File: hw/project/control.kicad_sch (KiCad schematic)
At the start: 46 parts, among them SW1 BOOT0, SW2 RESET, U1 STSPIN32G4, X1 32MHZ 10PF

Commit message: Place next tier of components after critical ones
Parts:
- removed TP4: REGIN, TestPoint:TestPoint_Pad_D1.0mm, symbol Connector:TestPoint
- removed TP8: VBAT, TestPoint:TestPoint_Pad_D1.0mm, symbol Connector:TestPoint
- renumbered TP2 to TP1, TP3 to TP2, TP5 to TP3, TP6 to TP4, TP7 to TP5, TP9 to TP6, TP10 to TP7, TP11 to TP8
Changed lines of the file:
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@@
 		(dnp no)
 		(fields_autoplaced yes)
-		(property "Reference" "TP6"
+		(property "Reference" "TP4"
 			(at 195.58 74.93 0)
 			(show_name no)
@@
 			(project "esc"
 				(path "/86a17c4d-db96-42a1-af84-d43fe593f4e6/50f7e8ea-49d2-4d3d-890c-dc3d94742dd9"
-					(reference "TP6")
+					(reference "TP4")
 					(unit 1)
 				)
@@
 		(dnp no)
 		(fields_autoplaced yes)
-		(property "Reference" "TP2"
+		(property "Reference" "TP1"
 			(at 185.42 29.2099 90)
 			(show_name no)
@@
 			(project "esc"
 				(path "/86a17c4d-db96-42a1-af84-d43fe593f4e6/50f7e8ea-49d2-4d3d-890c-dc3d94742dd9"
-					(reference "TP2")
+					(reference "TP1")
 					(unit 1)
 				)
@@
 		(dnp no)
 		(fields_autoplaced yes)
-		(property "Reference" "TP11"
+		(property "Reference" "TP8"
 			(at 162.56 152.9079 0)
 			(show_name no)
@@
 			(project "esc"
 				(path "/86a17c4d-db96-42a1-af84-d43fe593f4e6/50f7e8ea-49d2-4d3d-890c-dc3d94742dd9"
-					(reference "TP11")
+					(reference "TP8")
 					(unit 1)
 				)
@@
 	(symbol
 		(lib_id "Connector:TestPoint")
-		(at 170.18 68.58 0)
-		(unit 1)
-		(body_style 1)
-		(exclude_from_sim no)
-		(in_bom no)
-		(on_board yes)
-		(in_pos_files yes)
-		(dnp no)
-		(fields_autoplaced yes)
-		(property "Reference" "TP4"
-			(at 172.72 64.0079 0)
-			(show_name no)
-			(do_not_autoplace no)
-			(effects
-				(font
-					(size 1.27 1.27)
-				)
-				(justify left)
-			)
-		)
-		(property "Value" "REGIN"
-			(at 172.72 66.5479 0)
-			(show_name no)
-			(do_not_autoplace no)
-			(effects
-				(font
-					(size 1.27 1.27)
-				)
-				(justify left)
-			)
-		)
-		(property "Footprint" "TestPoint:TestPoint_Pad_D1.0mm"
-			(at 175.26 68.58 0)
-			(hide yes)
-			(show_name no)
-			(do_not_autoplace no)
-			(effects
-				(font
-					(size 1.27 1.27)
-				)
-			)
-		)
-		(property "Datasheet" ""
-			(at 175.26 68.58 0)
-			(hide yes)
-			(show_name no)
-			(do_not_autoplace no)
-			(effects
-				(font
-					(size 1.27 1.27)
-				)
-			)
-		)
-		(property "Description" "test point"
-			(at 170.18 68.58 0)
-			(hide yes)
-			(show_name no)
-			(do_not_autoplace no)
-			(effects
-				(font
-					(size 1.27 1.27)
-				)
-			)
-		)
-		(pin "1"
-		)
-		(instances
-			(project "esc"
-				(path "/86a17c4d-db96-42a1-af84-d43fe593f4e6/50f7e8ea-49d2-4d3d-890c-dc3d94742dd9"
-					(reference "TP4")
-					(unit 1)
-				)
-			)
-		)
-	)
-	(symbol
-		(lib_id "Connector:TestPoint")
 		(at 219.71 68.58 270)
 		(unit 1)
@@
 		(dnp no)
 		(fields_autoplaced yes)
-		(property "Reference" "TP5"
+		(property "Reference" "TP3"
 			(at 224.79 67.3099 90)
 			(show_name no)
@@
 			(project "esc"
 				(path "/86a17c4d-db96-42a1-af84-d43fe593f4e6/50f7e8ea-49d2-4d3d-890c-dc3d94742dd9"
-					(reference "TP5")
+					(reference "TP3")
 					(unit 1)
 				)
@@
 		(dnp no)
 		(fields_autoplaced yes)
-		(property "Reference" "TP10"
+		(property "Reference" "TP7"
 			(at 129.54 152.9079 0)
 			(show_name no)
@@
 			(project "esc"
 				(path "/86a17c4d-db96-42a1-af84-d43fe593f4e6/50f7e8ea-49d2-4d3d-890c-dc3d94742dd9"
-					(reference "TP10")
-					(unit 1)
-				)
-			)
-		)
-	)
-	(symbol
-		(lib_id "Connector:TestPoint")
-		(at 187.96 109.22 0)
-		(unit 1)
-		(body_style 1)
-		(exclude_from_sim no)
-		(in_bom no)
-		(on_board yes)
-		(in_pos_files yes)
-		(dnp no)
-		(fields_autoplaced yes)
-		(property "Reference" "TP8"
-			(at 190.5 104.6479 0)
-			(show_name no)
-			(do_not_autoplace no)
-			(effects
-				(font
-					(size 1.27 1.27)
-				)
-				(justify left)
-			)
-		)
-		(property "Value" "VBAT"
-			(at 190.5 107.1879 0)
-			(show_name no)
-			(do_not_autoplace no)
-			(effects
-				(font
-					(size 1.27 1.27)
-				)
-				(justify left)
-			)
-		)
-		(property "Footprint" "TestPoint:TestPoint_Pad_D1.0mm"
-			(at 193.04 109.22 0)
-			(hide yes)
-			(show_name no)
-			(do_not_autoplace no)
-			(effects
-				(font
-					(size 1.27 1.27)
-				)
-			)
-		)
-		(property "Datasheet" ""
-			(at 193.04 109.22 0)
-			(hide yes)
-			(show_name no)
-			(do_not_autoplace no)
-			(effects
-				(font
-					(size 1.27 1.27)
-				)
-			)
-		)
-		(property "Description" "test point"
-			(at 187.96 109.22 0)
-			(hide yes)
-			(show_name no)
-			(do_not_autoplace no)
-			(effects
-				(font
-					(size 1.27 1.27)
-				)
-			)
-		)
-		(pin "1"
-		)
-		(instances
-			(project "esc"
-				(path "/86a17c4d-db96-42a1-af84-d43fe593f4e6/50f7e8ea-49d2-4d3d-890c-dc3d94742dd9"
-					(reference "TP8")
+					(reference "TP7")
 					(unit 1)
 				)
@@
 		(dnp no)
 		(fields_autoplaced yes)
-		(property "Reference" "TP3"
+		(property "Reference" "TP2"
 			(at 143.51 67.3099 90)
 			(show_name no)
@@
 			(project "esc"
 				(path "/86a17c4d-db96-42a1-af84-d43fe593f4e6/50f7e8ea-49d2-4d3d-890c-dc3d94742dd9"
-					(reference "TP3")
+					(reference "TP2")
 					(unit 1)
 				)
@@
 		(dnp no)
 		(fields_autoplaced yes)
-		(property "Reference" "TP9"
+		(property "Reference" "TP6"
 			(at 147.32 114.3 0)
 			(show_name no)
@@
 			(project "esc"
 				(path "/86a17c4d-db96-42a1-af84-d43fe593f4e6/50f7e8ea-49d2-4d3d-890c-dc3d94742dd9"
-					(reference "TP9")
+					(reference "TP6")
 					(unit 1)
 				)
@@
 		(dnp no)
 		(fields_autoplaced yes)
-		(property "Reference" "TP7"
+		(property "Reference" "TP5"
 			(at 157.48 104.6479 0)
 			(show_name no)
@@
 			(project "esc"
 				(path "/86a17c4d-db96-42a1-af84-d43fe593f4e6/50f7e8ea-49d2-4d3d-890c-dc3d94742dd9"
-					(reference "TP7")
+					(reference "TP5")
 					(unit 1)
 				)

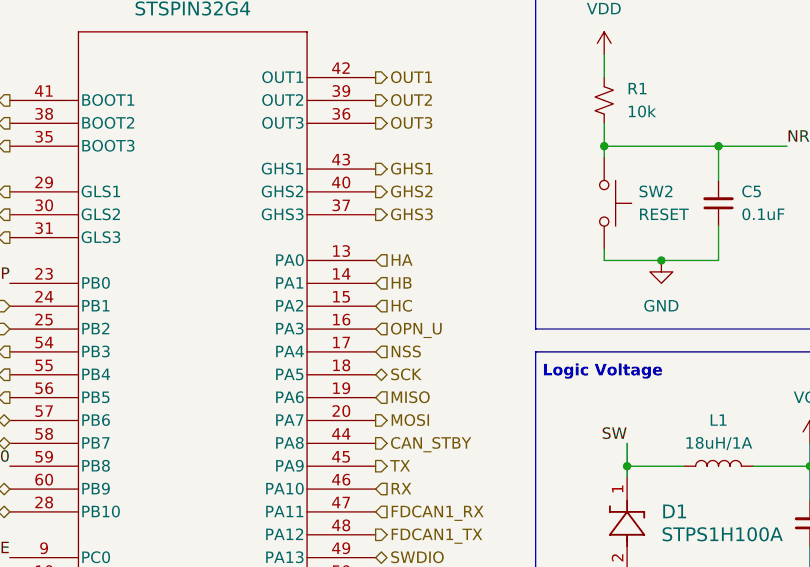
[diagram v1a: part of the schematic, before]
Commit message: Label JST connectors
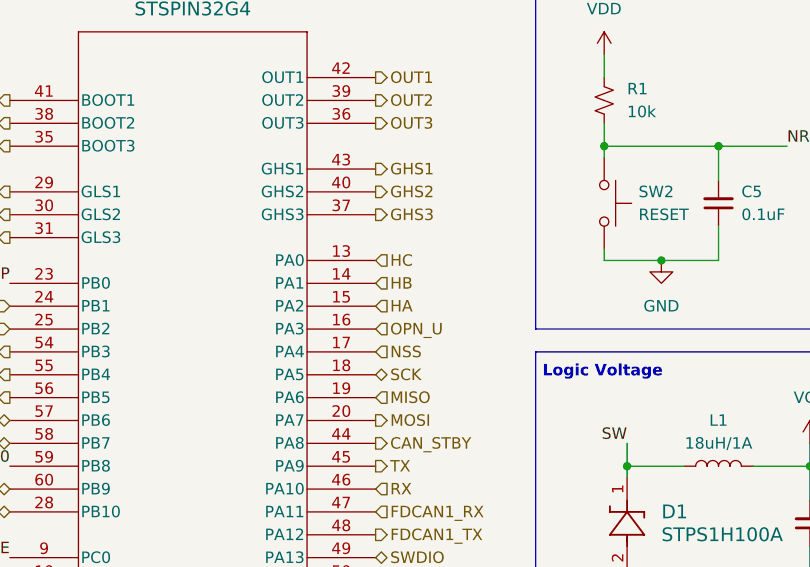
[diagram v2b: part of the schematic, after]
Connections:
- net HA: now also U1.15 (PA2); no longer U1.13 (PA0)
- net HC: now also U1.13 (PA0); no longer U1.15 (PA2)
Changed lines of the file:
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@@
 	(hierarchical_label "HC"
 		(shape input)
-		(at 73.66 50.8 0)
+		(at 73.66 45.72 0)
 		(effects
 			(font
@@
 	(hierarchical_label "HA"
 		(shape input)
-		(at 73.66 45.72 0)
+		(at 73.66 50.8 0)
 		(effects
 			(font

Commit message: Label everythangg
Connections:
- net HA: now also U1.13 (PA0); no longer U1.15 (PA2)
- net HC: now also U1.15 (PA2); no longer U1.13 (PA0)
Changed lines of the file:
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@@
 	(hierarchical_label "HC"
 		(shape input)
-		(at 73.66 45.72 0)
+		(at 73.66 50.8 0)
 		(effects
 			(font
@@
 	(hierarchical_label "HA"
 		(shape input)
-		(at 73.66 50.8 0)
+		(at 73.66 45.72 0)
 		(effects
 			(font

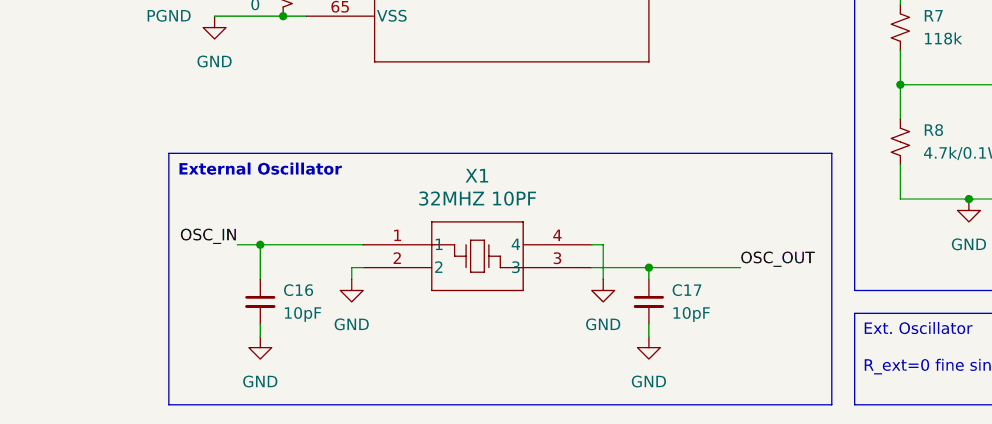
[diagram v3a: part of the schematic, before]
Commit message: Add LCSC field, update diode values/datasheets, crystal part
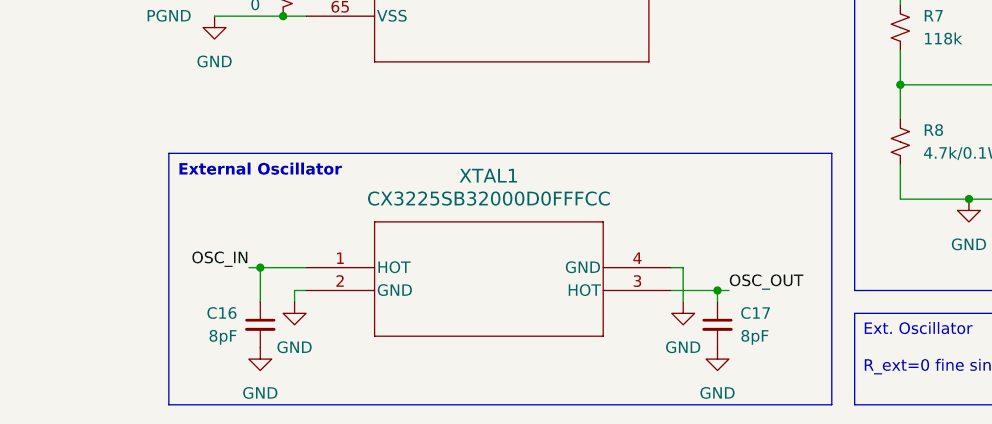
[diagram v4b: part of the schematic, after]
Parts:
- removed X1: 32MHZ 10PF, RH100_32_000_10_F_2020_EXT_TR:SMD4_RH100_2P5X3P2-2P2_RAL, symbol RH100_32_000_10_F_2020_EXT_TR:RH100-32.000-10-F-2020-EXT-TR
- added XTAL1: CX3225SB32000D0FFFCC, CX3225SB32000D0FFFCC:xtal4_CX3225SB_AVX, symbol CX3225SB32000D0FFFCC:CX3225SB32000D0FFFCC
- C16, C17: value 10pF -> 8pF
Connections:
- net GND: now also XTAL1.2 (GND), XTAL1.4 (GND)
- net OSC_IN: now also XTAL1.1 (HOT)
- net OSC_OUT: now also XTAL1.3 (HOT)
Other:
- moved on the sheet: C16

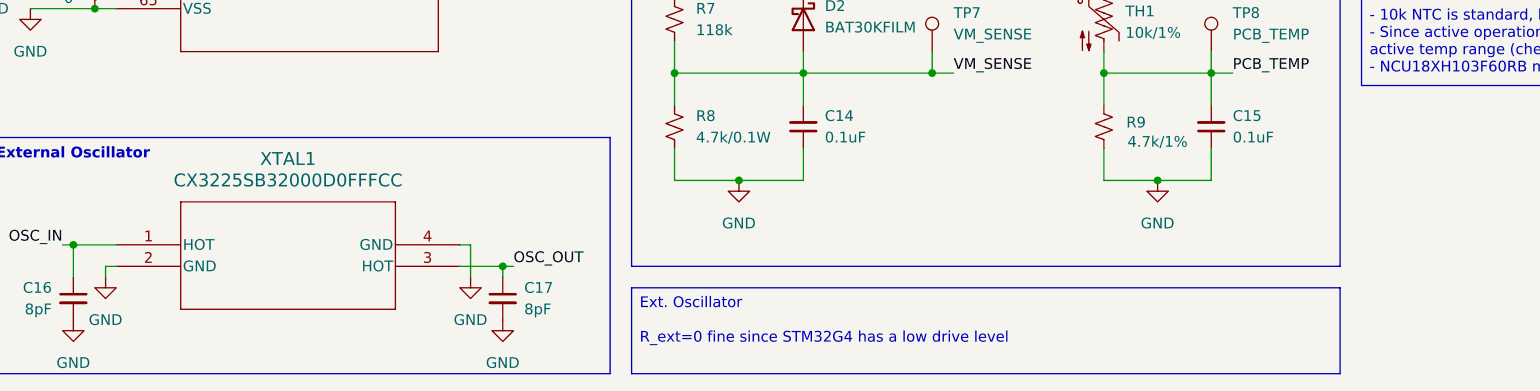
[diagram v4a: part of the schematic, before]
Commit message: Update bulk caps
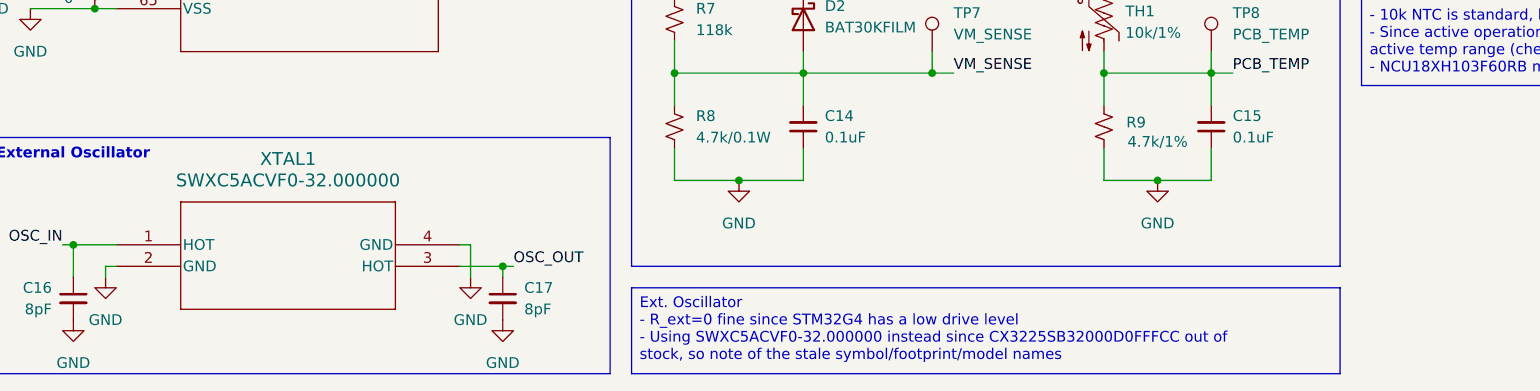
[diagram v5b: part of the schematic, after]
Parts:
- XTAL1: value CX3225SB32000D0FFFCC -> SWXC5ACVF0-32.000000; JLCPCB (none) -> https://jlcpcb.com/partdetail/Starwave-SWXC5ACVF0_32000000/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; LCSC (none) -> C22399832
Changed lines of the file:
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@@
 		)
 	)
-	(text_box "Ext. Oscillator\n\nR_ext=0 fine since STM32G4 has a low drive level"
+	(text_box "Ext. Oscillator\n- R_ext=0 fine since STM32G4 has a low drive level\n- Using SWXC5ACVF0-32.000000 instead since CX3225SB32000D0FFFCC out of stock, so note of the stale symbol/footprint/model names"
 		(exclude_from_sim no)
 		(at 91.44 185.4199 0)
@@
 			)
 		)
-		(property "Value" "CX3225SB32000D0FFFCC"
+		(property "Value" "SWXC5ACVF0-32.000000"
 			(at 50.8 172.72 0)
 			(show_name no)
@@
 			)
 		)
-		(property "Datasheet" "https://www.digikey.ca/en/products/detail/kyocera-avx/CX3225SB32000D0FFFCC/4896410?s=N4IgTCBcDaIMIA0DMYwFYDKAhFAGfAIrgGKlxwgC6AvkA"
+		(property "Datasheet" "https://jlcpcb.com/partdetail/Starwave-SWXC5ACVF0_32000000/C22399832"
 			(at 30.48 180.34 0)
 			(hide yes)
@@
 			)
 		)
-		(property "Description" "32 MHz ±10ppm Crystal 8pF 50 Ohms 4-SMD, No Lead"
+		(property "Description" "-40℃~+85℃ 32MHz 60Ω 8pF SMD crystal oscillator ±10ppm ±30ppm SMD3225-4P Crystals ROHS"
 			(at 30.48 180.34 0)
 			(hide yes)
@@
 			)
 		)
-		(property "LCSC" ""
+		(property "LCSC" "C22399832"
+			(at 30.48 180.34 0)
+			(hide yes)
+			(show_name no)
+			(do_not_autoplace no)
+			(effects
+				(font
+					(size 1.27 1.27)
+				)
+			)
+		)
+		(property "JLCPCB" "https://jlcpcb.com/partdetail/Starwave-SWXC5ACVF0_32000000/C22399832"
 			(at 30.48 180.34 0)
 			(hide yes)

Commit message: Update switches
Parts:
- removed SW1: BOOT0, SWT0220_016016GSA:SW_SWT0220-016016GSA_REVA, symbol Switch:SW_Push
- removed SW2: RESET, SWT0220_016016GSA:SW_SWT0220-016016GSA_REVA, symbol Switch:SW_Push
- added SW4: BOOT0, TS-1187A-B-A-B_XKB, symbol TS-1187A-B-A-B:TS-1187A-B-A-B
- added SW5: RESET, TS-1187A-B-A-B_XKB, symbol TS-1187A-B-A-B:TS-1187A-B-A-B
- TH1: JLCPCB (none) -> https://jlcpcb.com/partdetail/MurataElectronics-NCU18XH103F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; LCSC (none) -> C440252
- TP4, TP6: JLCPCB (none) -> https://jlcpcb.com/partdetail/Keystone-5016/C238129; LCSC (none) -> C238129
- U1: JLCPCB (none) -> https://jlcpcb.com/partdetail/STMicroelectronics-STSPIN32G4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; LCSC (none) -> C7434864
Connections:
- net GND: now also SW5.3, SW5.4
- net NRST: now also SW5.1, SW5.2
- net VDD: now also SW4.1, SW4.2
- net at R2.1, R3.1: now also SW4.3, SW4.4

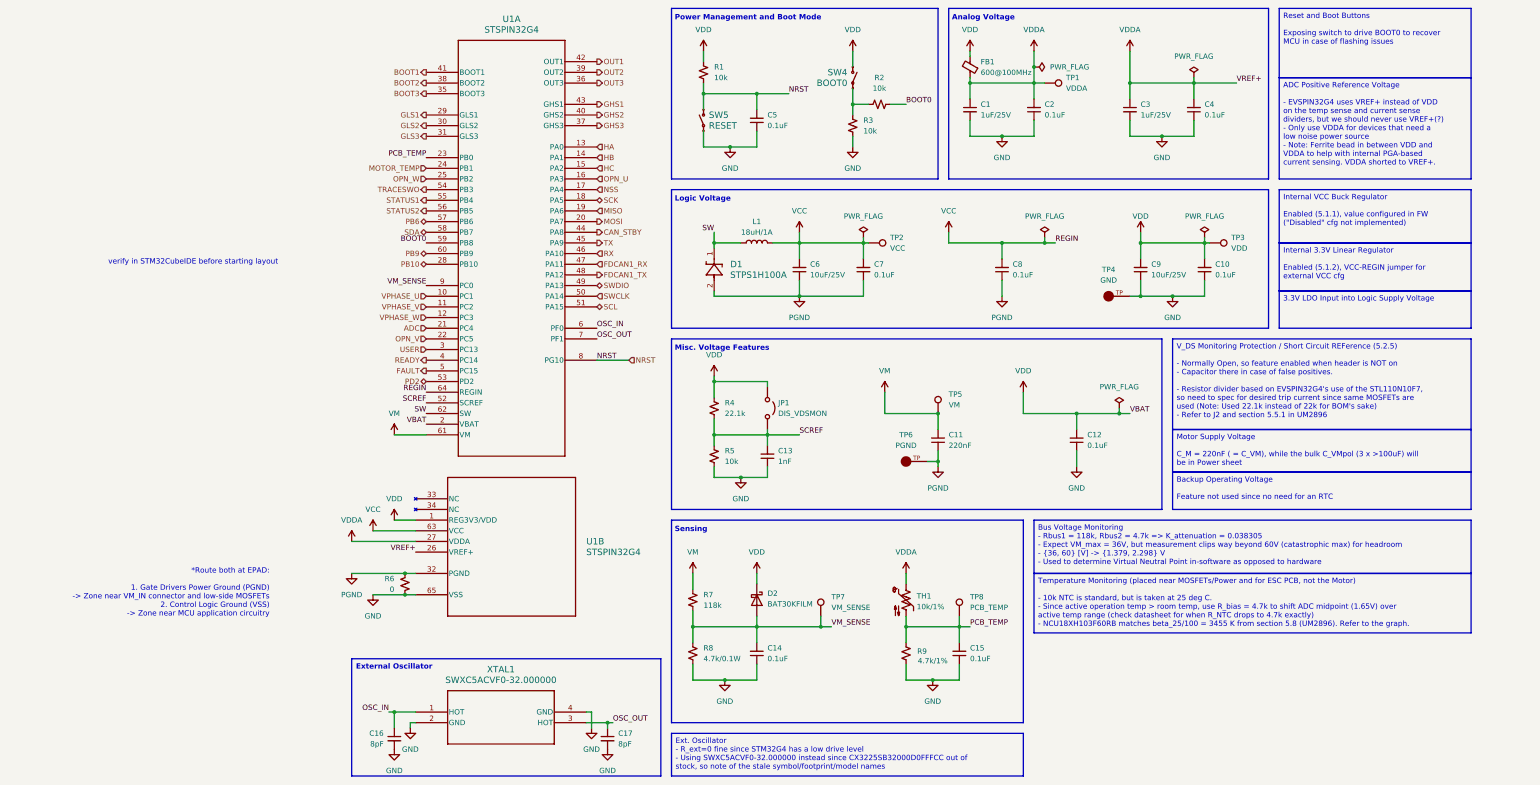
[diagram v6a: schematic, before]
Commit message: Spec everything with LCSC except for simple passives and header pins
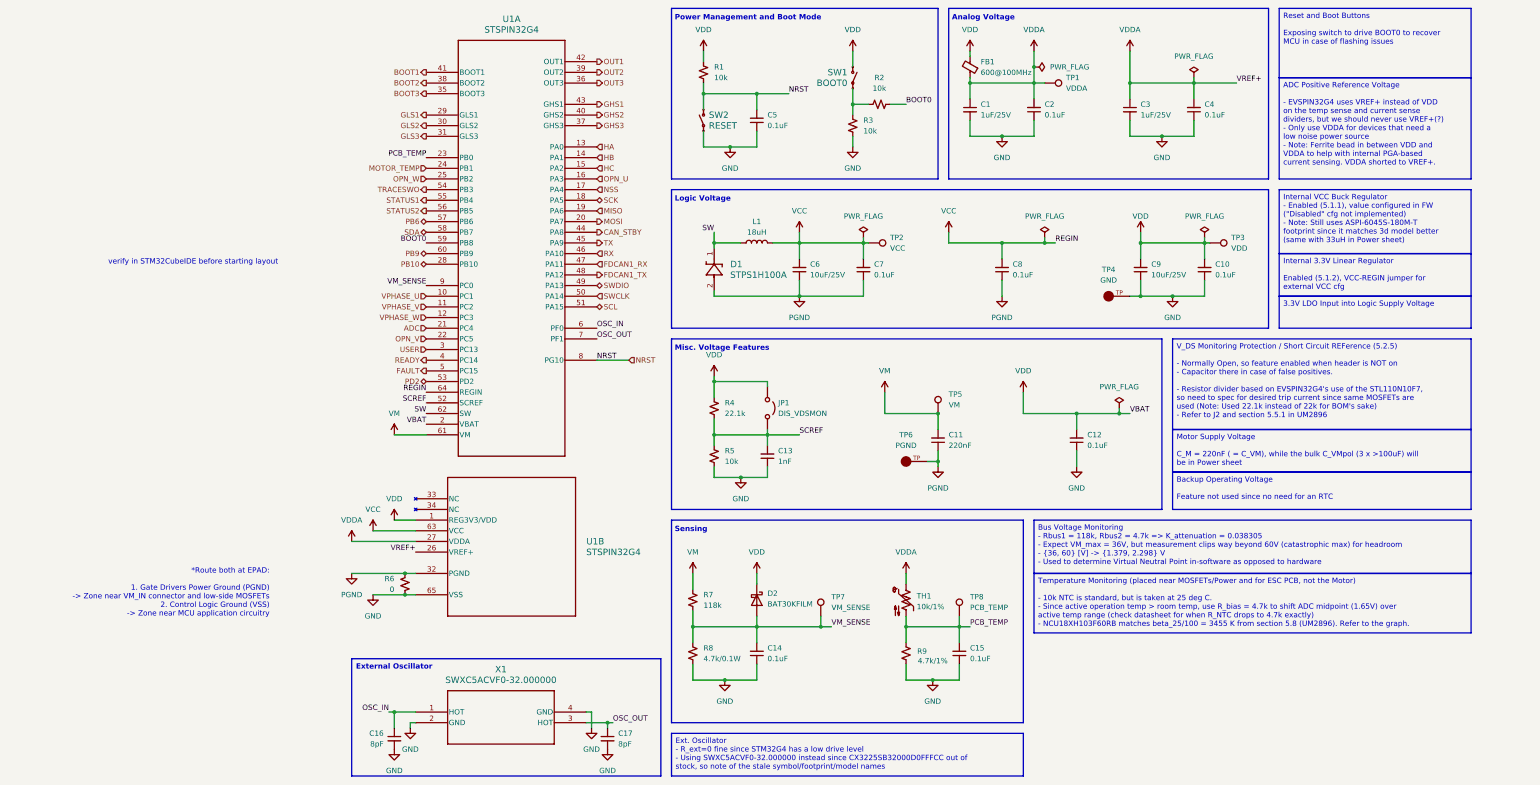
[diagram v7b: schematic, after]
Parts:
- removed XTAL1: SWXC5ACVF0-32.000000, CX3225SB32000D0FFFCC:xtal4_CX3225SB_AVX, symbol CX3225SB32000D0FFFCC:CX3225SB32000D0FFFCC
- added X1: SWXC5ACVF0-32.000000, CX3225SB32000D0FFFCC:xtal4_CX3225SB_AVX, symbol CX3225SB32000D0FFFCC:CX3225SB32000D0FFFCC
- C16, C17: JLCPCB (none) -> https://jlcpcb.com/partdetail/YAGEO-CC0603BRNPO9BN8R0/C5191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; LCSC (none) -> C519117
- D1: JLCPCB (none) -> https://jlcpcb.com/partdetail/STMicroelectronics-STPS1H100A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; LCSC (none) -> C165701
- D2: JLCPCB (none) -> https://jlcpcb.com/partdetail/STMicroelectronics-BAT30KFILM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; LCSC (none) -> C2926449
- FB1: JLCPCB (none) -> https://jlcpcb.com/partdetail/TAITECH-HCB1608KF601T20/C3043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; LCSC (none) -> C304319
- L1: value 18uH/1A -> 18uH; JLCPCB (none) -> https://jlcpcb.com/partdetail/Sunlord-SWPA6045S180MT/C96954; LCSC (none) -> C96954
- SW1: renamed from SW4; footprint TS-1187A-B-A-B_XKB -> TS-1187A-B-A-B:TS-1187A-B-A-B
- SW2: renamed from SW5; footprint TS-1187A-B-A-B_XKB -> TS-1187A-B-A-B:TS-1187A-B-A-B
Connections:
- net GND: now also X1.2 (GND), X1.4 (GND)
- net OSC_IN: now also X1.1 (HOT)
- net OSC_OUT: now also X1.3 (HOT)
